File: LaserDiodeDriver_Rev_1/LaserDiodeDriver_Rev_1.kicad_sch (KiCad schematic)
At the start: 0 parts

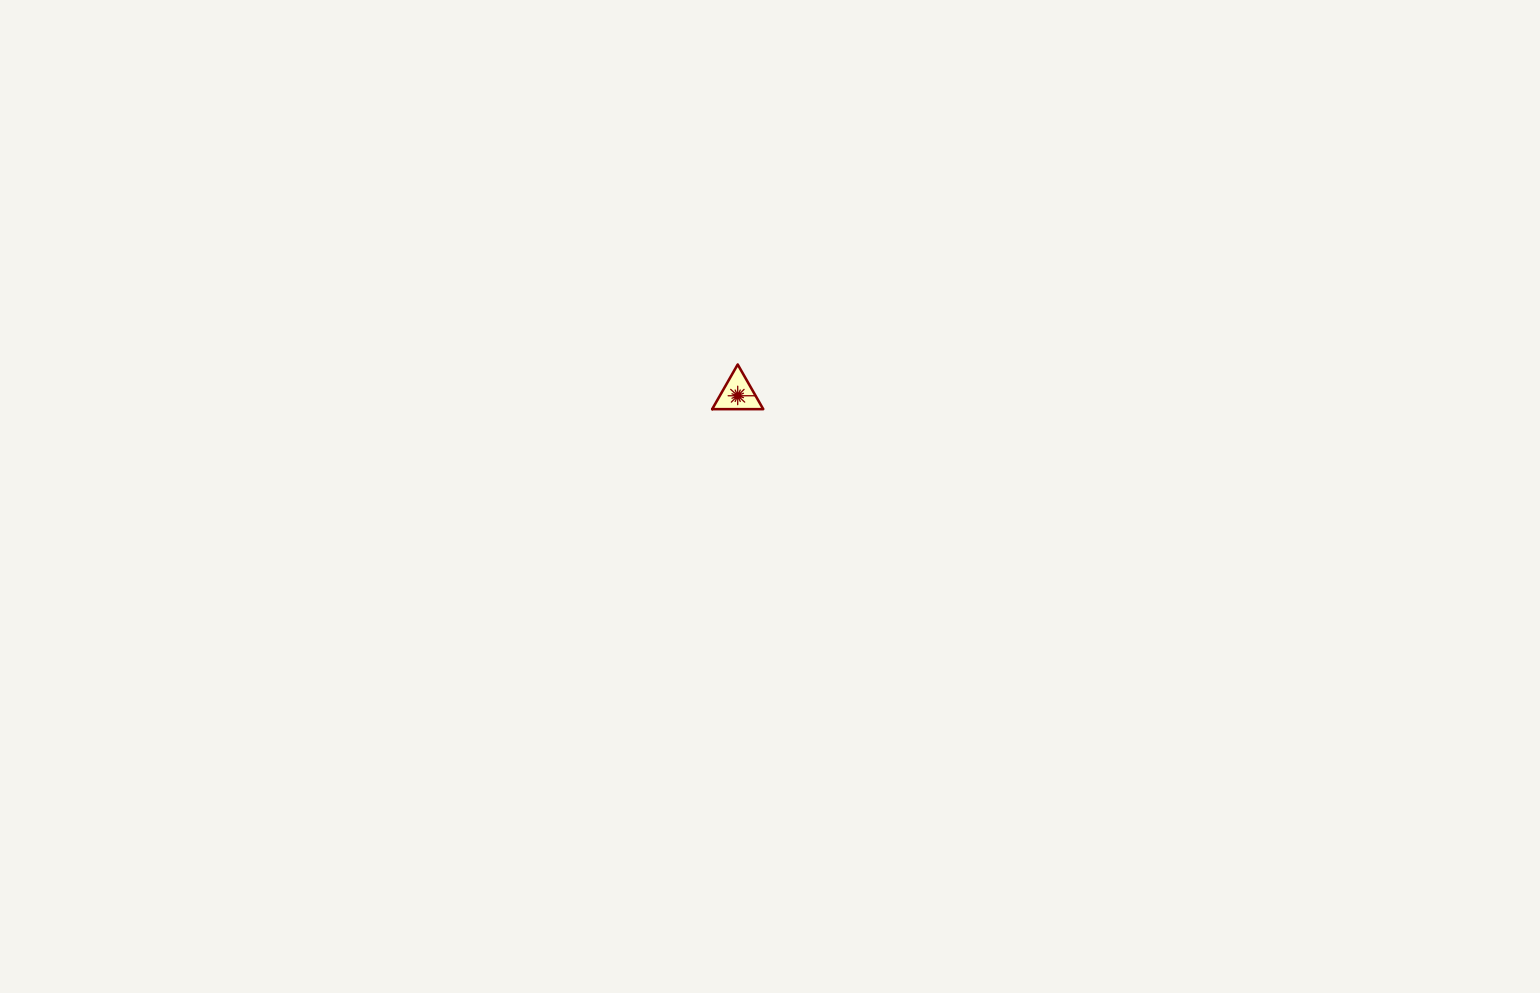
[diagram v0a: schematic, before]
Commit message: Added Transimpedance Amplifier
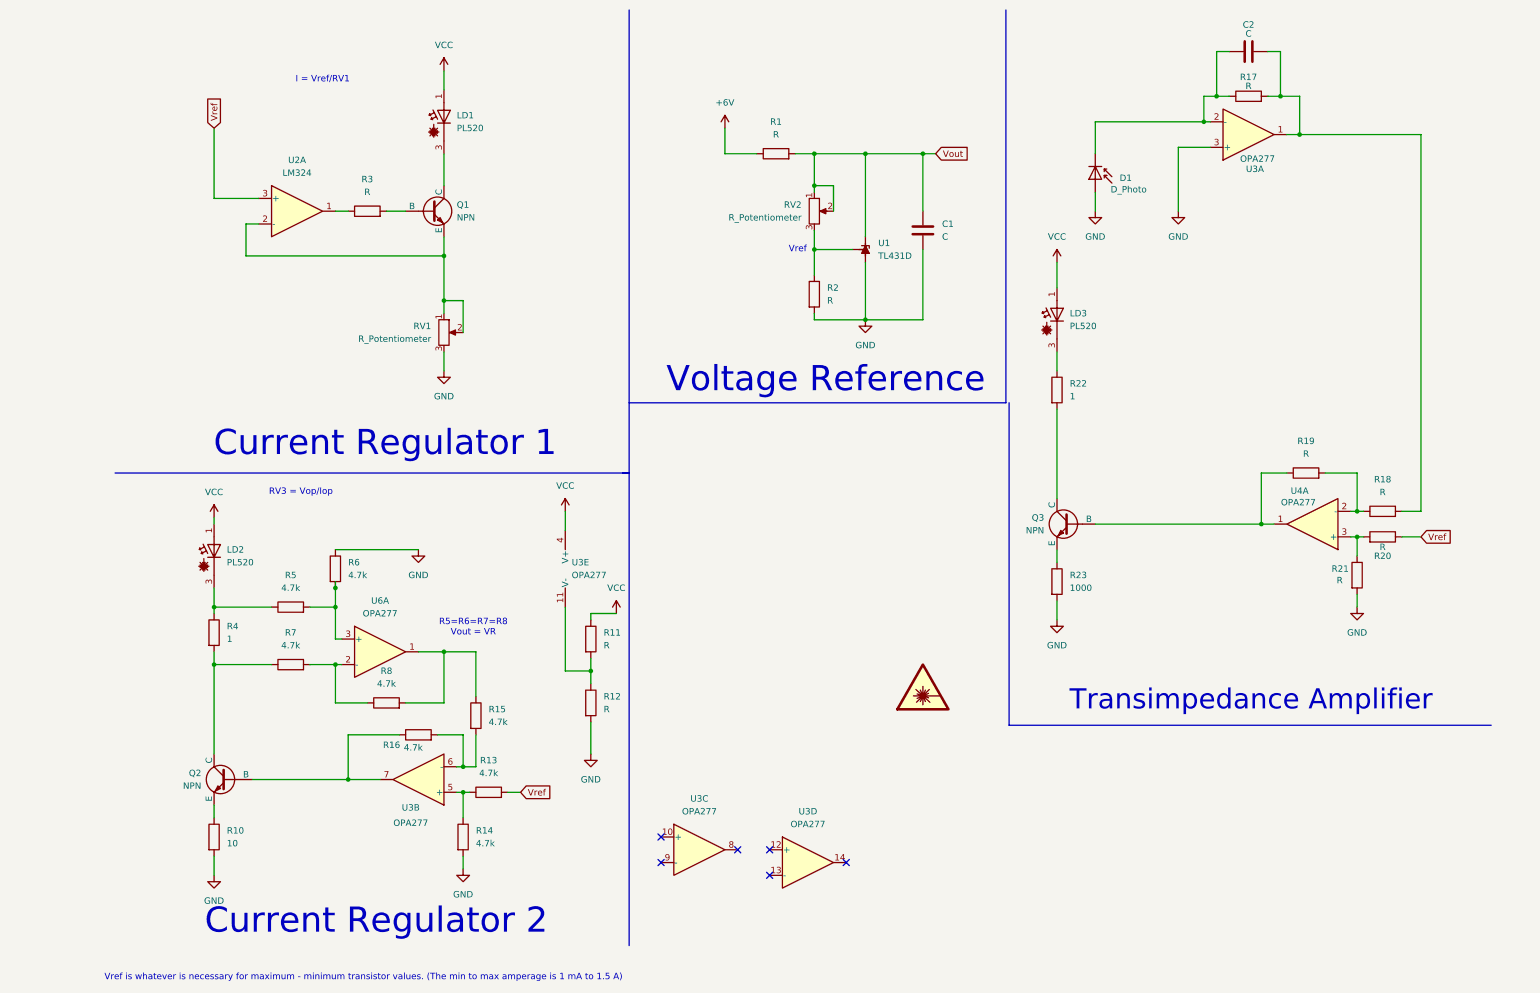
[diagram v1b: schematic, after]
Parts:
- added C1, C2: C, symbol Device:C
- added D1: D_Photo, symbol Device:D_Photo
- added LD1, LD2, LD3: PL520, OptoDevice:LaserDiode_TO38ICut-3, symbol Diode_Laser:PL520
- added Q1, Q2, Q3: NPN, symbol Simulation_SPICE:NPN
- added R1, R11, R12, R17, R18, R19, R2, R20, R21, R3: R, symbol Device:R
- added R10: 10, symbol Device:R
- added R13, R14, R15, R16, R5, R6, R7, R8: 4.7k, symbol Device:R
- added R22, R4: 1, Resistor_SMD:R_1206_3216Metric_Pad1.30x1.75mm_HandSolder, symbol Device:R
- added R23: 1000, symbol Device:R
- added RV1, RV2: R_Potentiometer, symbol Device:R_Potentiometer
- added U1: TL431D, Package_SO:SOIC-8_3.9x4.9mm_P1.27mm, symbol Reference_Voltage:TL431D
- added U2: LM324, symbol Amplifier_Operational:LM324
- added U3, U4, U6: OPA277, symbol Amplifier_Operational:LM324
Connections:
- new net: Q3.1 (C), R22.2
- new net: Q3.2 (B), R19.1, U4.1
- new net: Q3.3 (E), R23.1
- new net: R5.2, R6.2, U6.3 (+)
- new net: R2.1, RV2.3, U1.8 (REF)
- new net: Q2.1 (C), R4.2, R7.1
- new net: R7.2, R8.1, U6.2 (-)
- new net: LD2.3 (C), R4.1, R5.1
- new net: Q2.3 (E), R10.1
- new net: R15.1, R8.2, U6.1
- new net: R11.2, R12.1, U3.11 (V-)
- new net: LD3.3 (C), R22.1
- new net: Q2.2 (B), R16.1, U3.7
- new net: R15.2, R16.2, U3.6 (-)
- new net: LD1.3 (C), Q1.1 (C)
- new net: Q1.2 (B), R3.2
- new net: Q1.3 (E), RV1.1, RV1.2, U2.2 (-)
- new net: R3.1, U2.1
- new net: R20.2, R21.1, U4.3 (+)
- new net: C2.1, D1.1 (K), R17.1, U3.2 (-)
- new net: C2.2, R17.2, R18.2, U3.1
- new net: R13.1, R14.1, U3.5 (+)
- new net: R18.1, R19.2, U4.2 (-)
- new net +6V: R1.1
- new net GND: C1.2, D1.2 (A), R10.2, R12.2, R14.2, R2.2, R21.2, R23.2, R6.1, RV1.3, U1.2 (A), U1.3 (A), U1.6 (A), U1.7 (A), U3.3 (+)
- new net VCC: LD1.1 (A), LD2.1 (A), LD3.1 (A), R11.1, U3.4 (V+)
- new net Vout: C1.1, R1.2, RV2.1, RV2.2, U1.1 (K)
- new net Vref: R13.2, R20.1, U2.3 (+)
- no-connect marks 0 -> 6
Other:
- note added: "Current Regulator 1"
- note added: "Current Regulator 2"
- note added: "I = Vref/RV1"
- note added: "R5=R6=R7=R8 Vout = VR"
- note added: "RV3 = Vop/Iop"
- note added: "Transimpedance Amplifier"
- note added: "Voltage Reference"
- note added: "Vref"
- note added: "Vref is whatever is necessary for maximum - minimum transistor values. (The min to max amperage is 1 mA to 1.5 A)"

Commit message: Updated Laser Diode Driver
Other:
- note added: "Power Regulator"
- note added: "This Vref is the actual value we want to set the laser diode to"
- note removed: "RV3 = Vop/Iop"
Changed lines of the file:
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@@
 		)
 	)
-	(text "RV3 = Vop/Iop"
+	(text "Transimpedance Amplifier\n"
 		(exclude_from_sim no)
-		(at 49.022 107.95 0)
+		(at 241.046 48.514 0)
+		(effects
+			(font
+				(size 1.27 1.27)
+			)
+		)
+	)
+	(text "This Vref is the actual value we want to set the laser diode to\n"
+		(exclude_from_sim no)
+		(at 292.1 111.76 90)
 		(effects
 			(font
@@
 		)
 	)
-	(text "Transimpedance Amplifier"
+	(text "Power Regulator\n"
 		(exclude_from_sim no)
 		(at 237.998 149.352 0)
